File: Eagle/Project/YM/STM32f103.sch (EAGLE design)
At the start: 56 parts, among them IC1 YM3812, IC10 LM358D, IC11 YM3014B, IC12 LM358D, IC13 YM3812, IC14 YM3014B, IC15 LM358D, IC3 BA033CC0T, IC4 LM2575-5.0S, IC5 YM3812, IC6 YM3014B, IC7 YM3014B, IC8 LM358D, IC9 YM3812, U1 STM32F10XRXT6, X1 CRYSTALS-NOGND-4-HSMX

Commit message: PINOUT M3 CHECK
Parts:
- added J1: (no value), con-amp:MTA03-156
- added PL1: (no value), con-harting-v:16VS
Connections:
- net IO10 renamed ADC2
- net IO11 renamed ADC3
- net IO9 renamed ADC1
- net VOL-TOT renamed ADC-VOL-TOT
- net VOL1 renamed ADC-VOL1
- net VOL4 renamed ADC-VOL2
- new net N$16: J1.1
- new net N$17: J1.2
- new net N$18: J1.3
- net 3.3V: now also PL1-14.S
- net 5V: now also PL1-15.S
- net DAC-OUT-0: no longer IC12A.-IN, IC12A.OUT, IC15A.-IN, IC15A.OUT, IC8A.-IN, IC8A.OUT
- net DAC-OUT-1: now also IC8A.-IN, IC8A.OUT
- net DAC-OUT-2: now also IC12A.-IN, IC12A.OUT
- net DAC-OUT-3: now also IC15A.-IN, IC15A.OUT
- net EXP-RST: now also PL1-13.S
- net EXP-SPI-A0: now also PL1-7.S
- net EXP-SPI-A1: now also PL1-8.S
- net EXP-SPI-CLK: now also PL1-9.S
- net EXP-SPI-MISO: now also PL1-10.S
- net EXP-SPI-MOSI: now also PL1-11.S
- net EXP-SPI-NSS: now also PL1-12.S
- net EXP1-INTA: now also PL1-1.S
- net EXP1-INTB: now also PL1-2.S
- net EXP2-INTA: now also PL1-3.S
- net EXP2-INTB: now also PL1-4.S
- net EXP3-INTA: now also PL1-5.S
- net EXP3-INTB: now also PL1-6.S
- net GND: now also PL1-16.S

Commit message: Sheet OUTPUTS
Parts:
- added J2, J3, J4, J5, J6, J7, J8: (no value), con-amp:MTA03-156
- added X3: (no value), con-weidmueller-sl35:180G-14
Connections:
- removed net N$16: J1.1
- removed net N$17: J1.2
- removed net N$18: J1.3
- removed net VOL2: U1PORTC_L.PC4
- removed net VOL3: U1PORTC_L.PC5
- new net ADC-VOL3: J4.2, U1PORTC_L.PC5
- new net ADC-VOL4: J5.2, U1PORTB_L.PB0
- net 3.3V: now also J1.1, J2.1, J3.1, J4.1, J5.1, J6.1, J7.1, J8.1, X3.13, X3.2
- net 5V: now also X3.14, X3.3
- net ADC-VOL-TOT: now also J1.2
- net ADC-VOL1: now also J2.2
- net ADC-VOL2: now also J3.2, U1PORTC_L.PC4; no longer U1PORTB_L.PB0
- net ADC1: now also J6.2
- net ADC2: now also J7.2
- net ADC3: now also J8.2
- net GND: now also J1.3, J2.3, J3.3, J4.3, J5.3, J6.3, J7.3, J8.3, X3.1, X3.12
- net IO1: now also X3.11
- net IO2: now also X3.10
- net IO3: now also X3.9
- net IO4: now also X3.8
- net IO5: now also X3.7
- net IO6: now also X3.6
- net IO7: now also X3.5
- net IO8: now also X3.4
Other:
- moved on the sheet: J1, PL1-1, PL1-10, PL1-11, PL1-12, PL1-13, PL1-14, PL1-15, PL1-16, PL1-2, PL1-3, PL1-4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

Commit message: OUTPUT final
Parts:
- removed C1: (no value), rcl:C-EUC0603
- C2: value (none) -> 4.7uF
- C3, C4, C5, C6, C7: value (none) -> 10nF
- C8: value (none) -> 1uF
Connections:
- net 3.3V: no longer C1.1
- net GND: no longer C1.2
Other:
- moved on the sheet: C2, C3, C4, C5, C8

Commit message: Final merge
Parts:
- removed C34: 100UF, +HU-Lib:100UF
- removed C35: 330UF, +HU-Lib:330UF
- removed D1: 1N5819-B, diode:1N5819-B
- removed IC4: LM2575-5.0S, lm2575:LM2575-5.0S
- removed L1: 330UH, +HU-Lib:330UH
- added C36, C39, C40: 100nF, Clean-Kong:C-EUC0603
- added C37: 1p5F, Clean-Kong:C-EUC0603
- added C38: 4.7nF, Clean-Kong:C-EUC0603
- added CRYSTAL1: ABLS-3.579545MHZ-17-B-4-Y-T, ABLS-3.579545MHZ-17-B-4-Y-T:ABLS-3.579545MHZ-17-B-4-Y-T
- added D2: BAT20JFILM, BAT20JFILM:BAT20JFILM
- added J10: (no value), LDO:CON-USB-B
- added J9: DIN5, SparkFun-Connectors:DIN5
- added Q1: 6N136SDM, 6N136SDM:6N136SDM
- added R1: 91R, +HU-Lib:1K
- added R3, R4: 470R, +HU-Lib:1K
- added R5: 4k7, +HU-Lib:1K
- added U2: 74AC04MTC, 74AC04MTC:74AC04MTC
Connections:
- removed net 12V: C34.1, IC4.VIN
- removed net N$15: D1.C, IC4.OUT, L1.P$2
- new net N$16: D2.A, J9.5, Q1.VF-
- new net N$17: D2.C, Q1.VF+, R1.2
- new net N$18: C36.1, J9.2
- new net N$19: J9.4, R1.1
- new net N$20: CRYSTAL1.2, R3.2, U2.A0
- new net N$21: C37.2, Q1.VB
- new net N$22: CRYSTAL1.1, R4.2, U2.A2, U2.~O1
- new net N$23: C38.2, R3.1, U2.~O0
- new net N$24: C38.1, R4.1, U2.A1
- net 5V: now also C39.2, C40.2, J10.1, Q1.VCC, R5.1, U2.VCC; no longer C35.1, IC4.FB, L1.P$1
- net GND: now also C36.2, C37.1, C39.1, C40.1, J10.4, Q1.GND, U2.GND; no longer C34.2, C35.2, D1.A, IC4.GND, IC4.OFF
- net USART-RX: now also Q1.VO, R5.2
- net YM-CLK-I: now also U2.~O2
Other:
- note added: "Julian Schotborgh Klok voor YM3812"
- note added: "Julian Schotborgh MIDI aanlsuiting via optocoupler."
- moved on the sheet: C32, C33, IC3

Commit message: BRD created
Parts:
- removed C38: 4.7nF, Clean-Kong:C-EUC0603
- removed C39: 100nF, Clean-Kong:C-EUC0603
- removed IC14: YM3014B, YM:YM3014B
- removed IC15: LM358D, linear:LM358D
- added C1: 10nF, rcl:C-EUC0603
- added C34: 1p5F, Clean-Kong:C-EUC0603
- added IC2: YM3014B, YM:YM3014B
- added IC4: YM3812, YM:YM3812
- C12, C15, C16, C17: value 10UF -> 100N; device +HU-Lib:10UF -> +HU-Lib:100N
- C2: value 4.7uF -> 10nF
- C23, C24, C28, C29: value 100N -> 10UF; device +HU-Lib:100N -> +HU-Lib:10UF
- C31: value 100N -> 0.47UF; device +HU-Lib:100N -> +HU-Lib:0.47UF
- C32: value 0.47UF -> 22UF; device +HU-Lib:0.47UF -> +HU-Lib:22UF
- C33: value 22UF -> 100nF; device +HU-Lib:22UF -> Clean-Kong:C-EUC0603
- C36: value 100nF -> 4.7nF
- C37: value 1p5F -> 100nF
- C4: value 10nF -> 1uF
- C7: value 10nF -> 4.7uF
- C8: value 1uF -> 100N; device rcl:C-EUC0603 -> +HU-Lib:100N
- IC10: value LM358D -> YM3812; device linear:LM358D -> YM:YM3812
- IC13: value YM3812 -> BA033CC0T; device YM:YM3812 -> LDO:VREG_MULTI
- IC3: value BA033CC0T -> LM358D; device LDO:VREG_MULTI -> linear:LM358D
- IC5: value YM3812 -> YM3014B; device YM:YM3812 -> YM:YM3014B
- IC6: value YM3014B -> LM358D; device YM:YM3014B -> linear:LM358D
- IC7: value YM3014B -> YM3812; device YM:YM3014B -> YM:YM3812
- IC8: value LM358D -> YM3014B; device linear:LM358D -> YM:YM3014B
- IC9: value YM3812 -> LM358D; device YM:YM3812 -> linear:LM358D
- J1: device con-amp:MTA03-156 -> LDO:CON-USB-B
- J10: device LDO:CON-USB-B -> con-amp:MTA03-156
- J2: value (none) -> DIN5; device con-amp:MTA03-156 -> SparkFun-Connectors:DIN5
- J9: value DIN5 -> (none); device SparkFun-Connectors:DIN5 -> con-amp:MTA03-156
- R1: value 91R -> 1K
- R2: value 1K -> 91R
- R3: value 470R -> 4k7
- R5: value 4k7 -> 470R
- renumbered C40 to C35, D2 to D1, JP2 to JP1, X3 to X2
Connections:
- removed net N$12 (its old number): IC14.BUFF, IC15A.+IN
- new net N$9: IC8.BUFF, IC9A.+IN
- net 3.3V: now also C1.1, C32.1, IC13.OUT, J10.1, J9.1, R1.2; no longer C33.1, C8.1, IC3.OUT, J1.1, J2.1, R2.2
- net 5V: now also C11.1, C12.1, C15.1, C16.1, C17.1, C37.2, IC10./RD, IC10.VCC, IC13.IN, IC2.VDD, IC3P.V+, IC4./RD, IC4.VCC, IC5.VDD, IC6P.V+, IC7./RD, IC7.VCC, IC8.VDD, IC9P.V+, J1.1, R3.1; no longer C23.1, C24.1, C28.1, C29.1, C32.1, C39.2, IC10P.V+, IC13./RD, IC13.VCC, IC14.VDD, IC15P.V+, IC3.IN, IC5./RD, IC5.VCC, IC6.VDD, IC7.VDD, IC8P.V+, IC9./RD, IC9.VCC, J10.1, R5.1
- net ADC-VOL-TOT: now also J3.2; no longer J1.2
- net ADC-VOL1: now also J4.2; no longer J2.2
- net ADC-VOL2: now also J5.2; no longer J3.2
- net ADC-VOL3: now also J6.2; no longer J4.2
- net ADC-VOL4: now also J7.2; no longer J5.2
- net ADC1: now also J8.2; no longer J6.2
- net ADC2: now also J9.2; no longer J7.2
- net ADC3: now also J10.2; no longer J8.2
- net DAC-OUT-0: now also IC3A.-IN, IC3A.OUT; no longer IC10A.-IN, IC10A.OUT
- net DAC-OUT-1: now also IC6A.-IN, IC6A.OUT; no longer IC8A.-IN, IC8A.OUT
- net DAC-OUT-2: now also IC9A.-IN, IC9A.OUT; no longer IC12A.-IN, IC12A.OUT
- net DAC-OUT-3: now also IC12A.-IN, IC12A.OUT; no longer IC15A.-IN, IC15A.OUT
- net GND: now also C1.2, C34.1, IC10.GND, IC13.GND1, IC13.GND2, IC2.GND, IC3P.V-, IC4.GND, IC6P.V-, IC8.GND, IC9P.V-, J1.4, J10.3, J9.3; no longer C36.2, C39.1, IC10P.V-, IC13.GND, IC14.GND, IC15P.V-, IC3.GND1, IC3.GND2, IC6.GND, IC8P.V-, IC9.GND, J1.3, J10.4, J2.3
- net N$10: now also C24.1, IC8.MP, IC9B.-IN; no longer C17.1, IC11.MP, IC12B.+IN
- net N$11: now also C23.1, IC8.RB, IC9B.+IN, IC9B.OUT; no longer C16.1, IC11.RB, IC12B.-IN, IC12B.OUT
- net N$13: now also C29.1, IC11.MP, IC12B.-IN; no longer C19.1, IC14.MP, IC15B.+IN
- net N$14: now also C28.1, IC11.RB, IC12B.+IN, IC12B.OUT; no longer C18.1, IC14.RB, IC15B.-IN, IC15B.OUT
- net N$16: now also J2.5; no longer J9.5
- net N$17: now also R2.2; no longer R1.2
- net N$18: now also C33.1, J2.2; no longer C36.1, J9.2
- net N$19: now also J2.4, R2.1; no longer J9.4, R1.1
- net N$20: now also R4.2; no longer R3.2
- net N$21: now also C34.2; no longer C37.2
- net N$22: now also R5.2; no longer R4.2
- net N$23: now also C36.2, R4.1; no longer C38.2, R3.1
- net N$24: now also C36.1, R5.1; no longer C38.1, R4.1
- net N$3: now also IC2.BUFF, IC3A.+IN; no longer IC10A.+IN, IC6.BUFF
- net N$4: now also C14.1, IC2.MP, IC3B.-IN; no longer C13.1, IC10B.+IN, IC6.MP
- net N$5: now also C13.1, IC2.RB, IC3B.+IN, IC3B.OUT; no longer C12.1, IC10B.-IN, IC10B.OUT, IC6.RB
- net N$6: now also IC5.BUFF, IC6A.+IN; no longer IC7.BUFF, IC8A.+IN
- net N$7: now also C19.1, IC5.MP, IC6B.-IN; no longer C15.1, IC7.MP, IC8B.+IN
- net N$8: now also C18.1, IC5.RB, IC6B.+IN, IC6B.OUT; no longer C14.1, IC7.RB, IC8B.-IN, IC8B.OUT
- net RST: now also C8.1, R1.1; no longer C11.1, R2.1
- net USART-RX: now also R3.2; no longer R5.2
- net YM-A0: now also IC10.A0, IC4.A0, IC7.A0; no longer IC13.A0, IC5.A0, IC9.A0
- net YM-CLK-I: now also IC10.M, IC4.M, IC7.M; no longer IC13.M, IC5.M, IC9.M
- net YM-CLK-O1: now also IC2.CLK; no longer IC6.CLK
- net YM-CLK-O2: now also IC4.SY, IC5.CLK; no longer IC5.SY, IC7.CLK
- net YM-CLK-O3: now also IC7.SY, IC8.CLK; no longer IC11.CLK, IC9.SY
- net YM-CLK-O4: now also IC10.SY, IC11.CLK; no longer IC13.SY, IC14.CLK
- net YM-CS2: now also IC4./CS; no longer IC5./CS
- net YM-CS3: now also IC7./CS; no longer IC9./CS
- net YM-CS4: now also IC10./CS; no longer IC13./CS
- net YM-D0: now also IC10.D0, IC4.D0, IC7.D0; no longer IC13.D0, IC5.D0, IC9.D0
- net YM-D1: now also IC10.D1, IC4.D1, IC7.D1; no longer IC13.D1, IC5.D1, IC9.D1
- net YM-D2: now also IC10.D2, IC4.D2, IC7.D2; no longer IC13.D2, IC5.D2, IC9.D2
- net YM-D3: now also IC10.D3, IC4.D3, IC7.D3; no longer IC13.D3, IC5.D3, IC9.D3
- net YM-D4: now also IC10.D4, IC4.D4, IC7.D4; no longer IC13.D4, IC5.D4, IC9.D4
- net YM-D5: now also IC10.D5, IC4.D5, IC7.D5; no longer IC13.D5, IC5.D5, IC9.D5
- net YM-D6: now also IC10.D6, IC4.D6, IC7.D6; no longer IC13.D6, IC5.D6, IC9.D6
- net YM-D7: now also IC10.D7, IC4.D7, IC7.D7; no longer IC13.D7, IC5.D7, IC9.D7
- net YM-RST: now also IC10./IC, IC4./IC, IC7./IC; no longer IC13./IC, IC5./IC, IC9./IC
- net YM-WR: now also IC10./WR, IC4./WR, IC7./WR; no longer IC13./WR, IC5./WR, IC9./WR
- net YM0-OUTPUT: now also IC10.MO, IC2.SD, IC4.MO, IC5.SD, IC7.MO, IC8.SD; no longer IC13.MO, IC14.SD, IC5.MO, IC6.SD, IC7.SD, IC9.MO
- net YM0-SYNC: now also IC10.SH, IC2.LOAD, IC4.SH, IC5.LOAD, IC7.SH, IC8.LOAD; no longer IC13.SH, IC14.LOAD, IC5.SH, IC6.LOAD, IC7.LOAD, IC9.SH

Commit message: FINAL VERSION - DAC NOG NIET GECONNECT
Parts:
- removed C36: 4.7nF, Clean-Kong:C-EUC0603
- removed C37: 100nF, Clean-Kong:C-EUC0603
- removed CRYSTAL1: ABLS-3.579545MHZ-17-B-4-Y-T, ABLS-3.579545MHZ-17-B-4-Y-T:ABLS-3.579545MHZ-17-B-4-Y-T
- removed Q1: 6N136SDM, 6N136SDM:6N136SDM
- removed R4, R5: 470R, +HU-Lib:1K
- removed U2: 74AC04MTC, 74AC04MTC:74AC04MTC
- added C38: 4.7nF, Clean-Kong:C-EUC0603
- added C39: 100nF, Clean-Kong:C-EUC0603
- added CRYSTAL2: ABLS-3.579545MHZ-17-B-4-Y-T, ABLS-3.579545MHZ-17-B-4-Y-T:ABLS-3.579545MHZ-17-B-4-Y-T
- added IC14: 74ALS04N, 74xx-us:74ALS04N
- added IC15: 6N136, 6N136:6N136
- added R6, R7: 470R, +HU-Lib:1K
- IC12, IC3, IC6, IC9: value LM358D -> LM358N; device linear:LM358D -> linear:LM358N
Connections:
- removed net N$22: CRYSTAL1.1, R5.2, U2.A2, U2.~O1
- removed net N$23: C36.2, R4.1, U2.~O0
- removed net N$24: C36.1, R5.1, U2.A1
- new net N$25: C38.2, IC14A.O, R6.1
- new net N$26: C38.1, IC14B.I, R7.1
- new net N$27: CRYSTAL2.2, IC14A.I, R6.2
- new net N$28: C39.2
- net 5V: now also IC14P.VCC, IC15.C(VCC); no longer C37.2, Q1.VCC, U2.VCC
- net GND: now also C39.1, IC14P.GND, IC15.E(GND), JP1.6; no longer C37.1, JP1.5, Q1.GND, U2.GND
- net N$16: now also IC15.C; no longer Q1.VF-
- net N$17: now also IC15.A; no longer Q1.VF+
- net N$20: now also CRYSTAL2.1, IC14B.O, IC14C.I, R7.2; no longer CRYSTAL1.2, R4.2, U2.A0
- net N$21: now also IC15.B(VB); no longer Q1.VB
- net USART-RX: now also IC15.C(VO); no longer Q1.VO
- net YM-CLK-I: now also IC14C.O; no longer U2.~O2

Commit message: DIG OUTPUT-PINNEN
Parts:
- removed JP1: (no value), adafruit:PINHD-1X6
- added SL1: (no value), con-amp-quick:M12
- added SL2: (no value), con-amp-quick:M06
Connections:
- net YM-CS3 renamed YM3-CS
- net YM-CS4 renamed YM4-CS
- removed net YM-CLK-O1: IC1.SY, IC2.CLK
- removed net YM-CLK-O2: IC4.SY, IC5.CLK
- removed net YM-CLK-O3: IC7.SY, IC8.CLK
- removed net YM-CLK-O4: IC10.SY, IC11.CLK
- removed net YM-CS1: IC1./CS, U1PORTA_H.PA15
- removed net YM-CS2: IC4./CS, U1PORTC_H.PC10
- removed net YM0-OUTPUT: IC1.MO, IC10.MO, IC11.SD, IC2.SD, IC4.MO, IC5.SD, IC7.MO, IC8.SD
- removed net YM0-SYNC: IC1.SH, IC10.SH, IC11.LOAD, IC2.LOAD, IC4.SH, IC5.LOAD, IC7.SH, IC8.LOAD
- new net YM1-CLK-O: IC1.SY, IC2.CLK, SL1.1
- new net YM1-CS: IC1./CS, U1PORTA_H.PA15, U1PORTC_H.PC10
- new net YM1-OUTPUT: IC1.MO, IC2.SD, SL1.5
- new net YM1-SYNC: IC1.SH, IC2.LOAD, SL1.9
- new net YM2-CLK-O: IC4.SY, IC5.CLK, SL1.2
- new net YM2-CS: IC4./CS
- new net YM2-OUTPUT: IC4.MO, IC5.SD, SL1.6
- new net YM2-SYNC: IC4.SH, IC5.LOAD, SL1.10
- new net YM3-CLK-O: IC7.SY, IC8.CLK, SL1.3
- new net YM3-OUTPUT: IC7.MO, IC8.SD, SL1.7
- new net YM3-SYNC: IC7.SH, IC8.LOAD, SL1.11
- new net YM4-CLK-O: IC10.SY, IC11.CLK, SL1.4
- new net YM4-OUTPUT: IC10.MO, IC11.SD, SL1.8
- new net YM4-SYNC: IC10.SH, IC11.LOAD, SL1.12
- net DAC-OUT-0: now also SL2.1; no longer JP1.1
- net DAC-OUT-1: now also SL2.2; no longer JP1.2
- net DAC-OUT-2: now also SL2.3; no longer JP1.3
- net DAC-OUT-3: now also SL2.4; no longer JP1.4
- net GND: now also SL2.6; no longer JP1.6
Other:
- moved on the sheet: X2

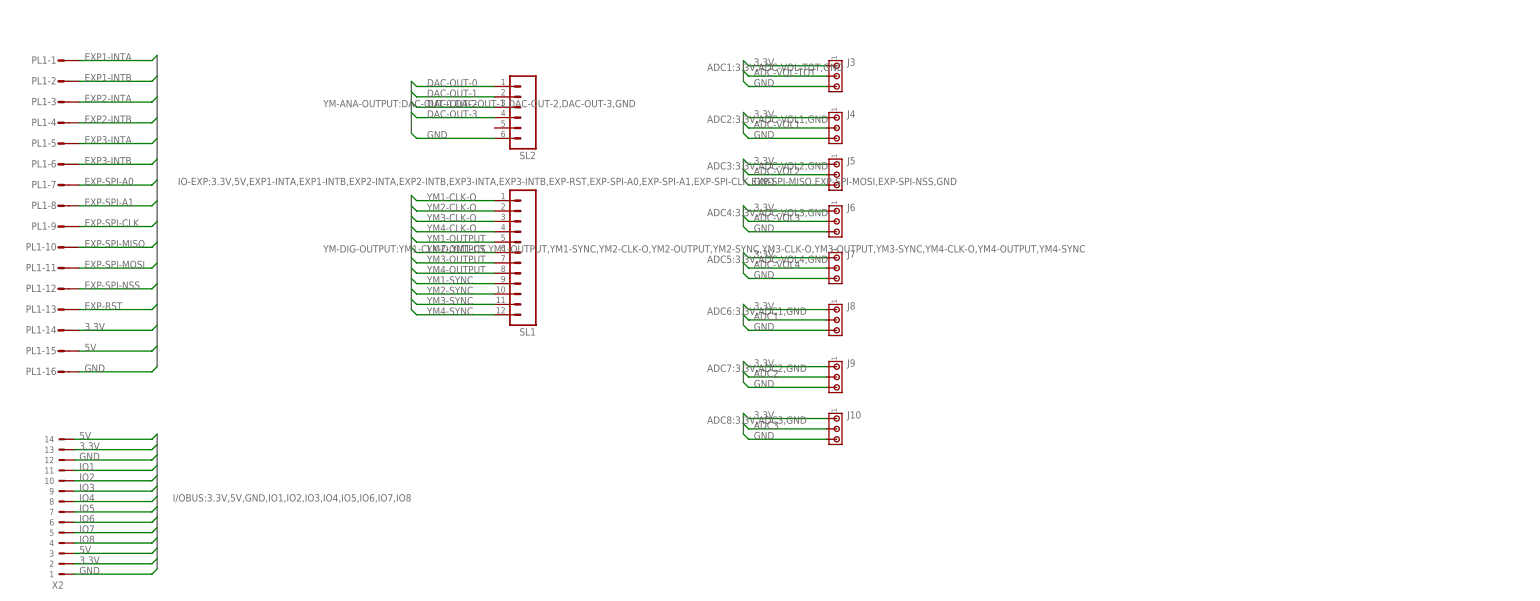
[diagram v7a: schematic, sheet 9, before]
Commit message: M4 - pin extended
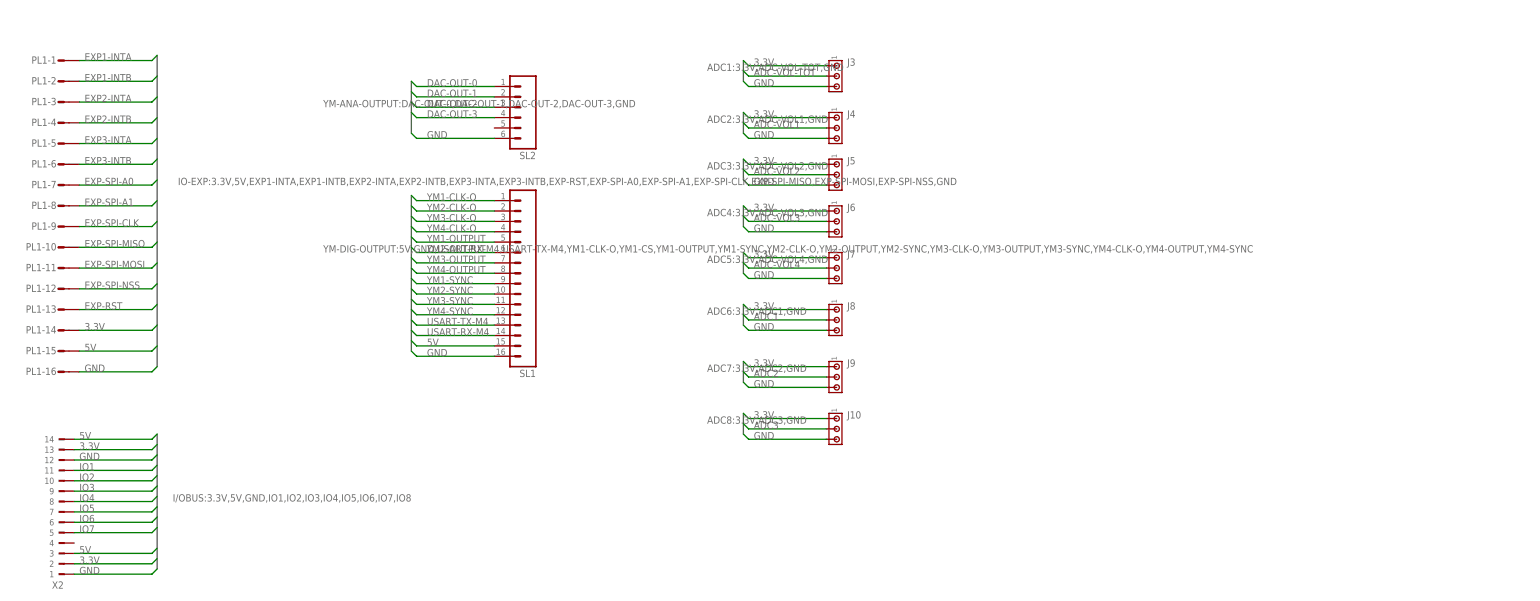
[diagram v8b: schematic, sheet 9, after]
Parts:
- SL1: device con-amp-quick:M12 -> con-amp-quick:M16
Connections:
- removed net IO8: U1PORTA_L.PA3, X2.4
- removed net USART-RX: IC15.C(VO), R3.2, U1PORTB_H.PB11
- removed net USART-TX: U1PORTB_H.PB10
- new net USART-RX-M4: SL1.14, U1PORTB_H.PB11
- new net USART-RX-MIDI: IC15.C(VO), R3.2, U1PORTA_L.PA3
- new net USART-TX-M4: SL1.13, U1PORTB_H.PB10
- net 5V: now also SL1.15
- net GND: now also SL1.16
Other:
- moved on the sheet: C35
